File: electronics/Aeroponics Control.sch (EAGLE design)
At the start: 37 parts, among them IC1 7407N, K1 SRM-1C-SL-5VDC, K2 SRM-1C-SL-5VDC, Q1 FDU3N40TU, Q2 FDU3N40TU, Q3 FDU3N40TU, Q4 FDU3N40TU, Q6 FDU3N40TU, Q7 FDU3N40TU

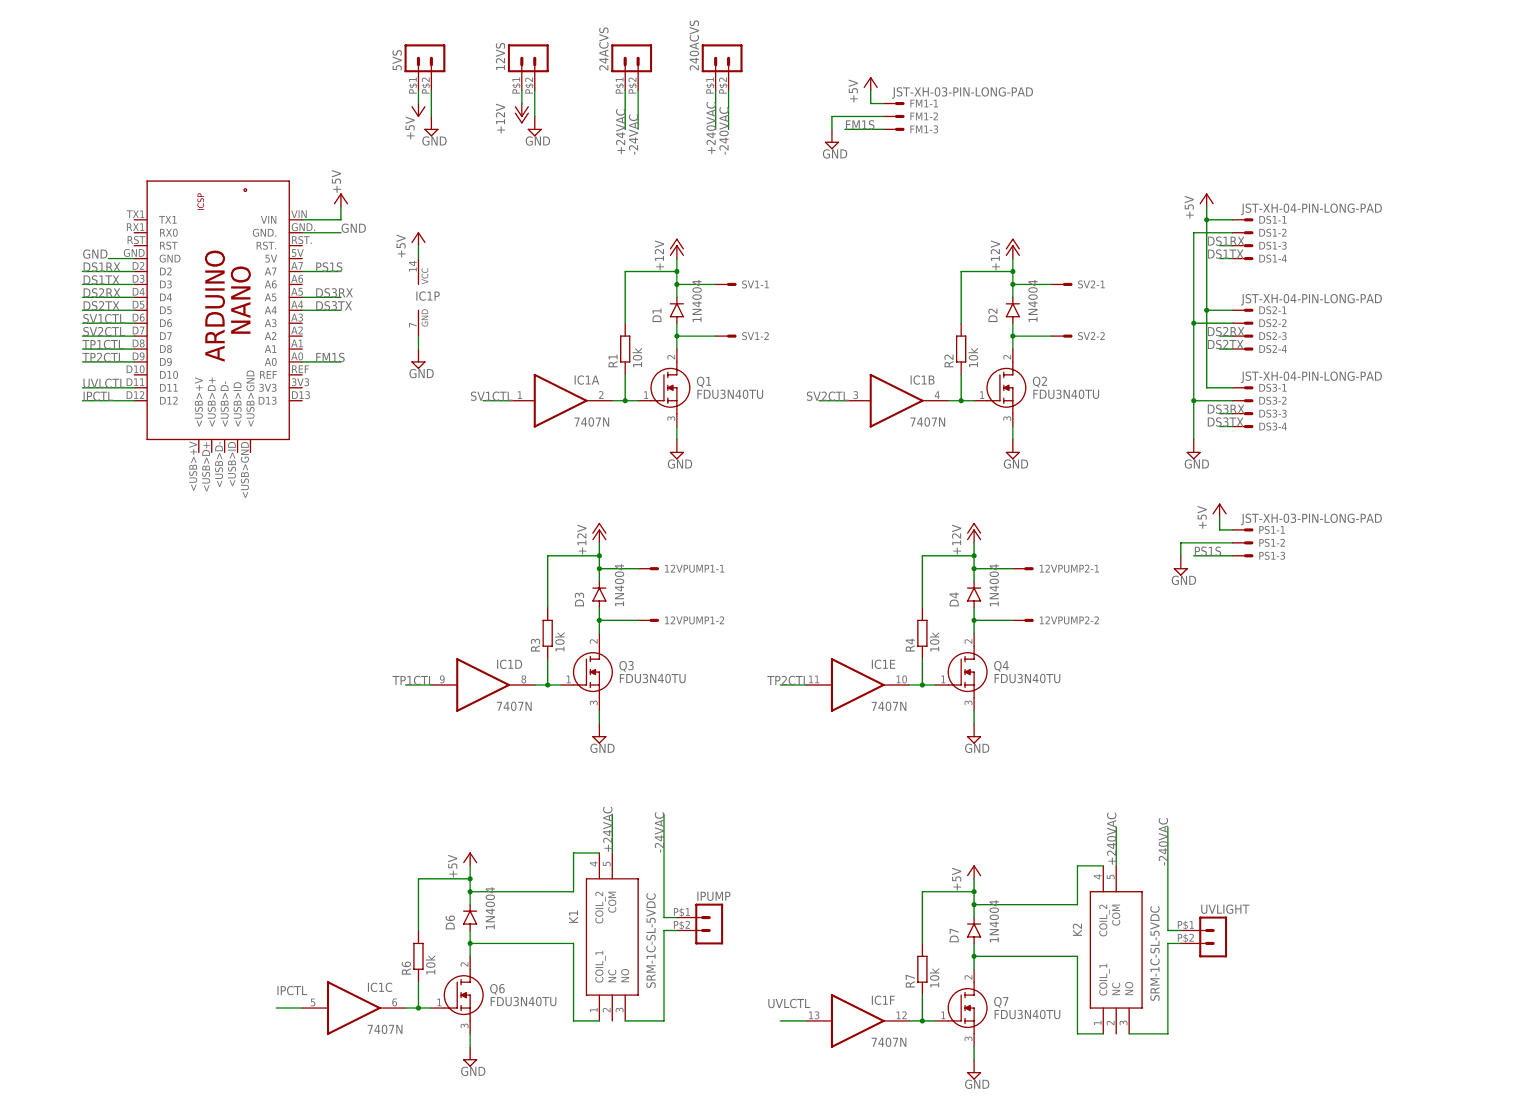
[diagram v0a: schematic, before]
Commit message: Electronics tested. Added calibration and debug.
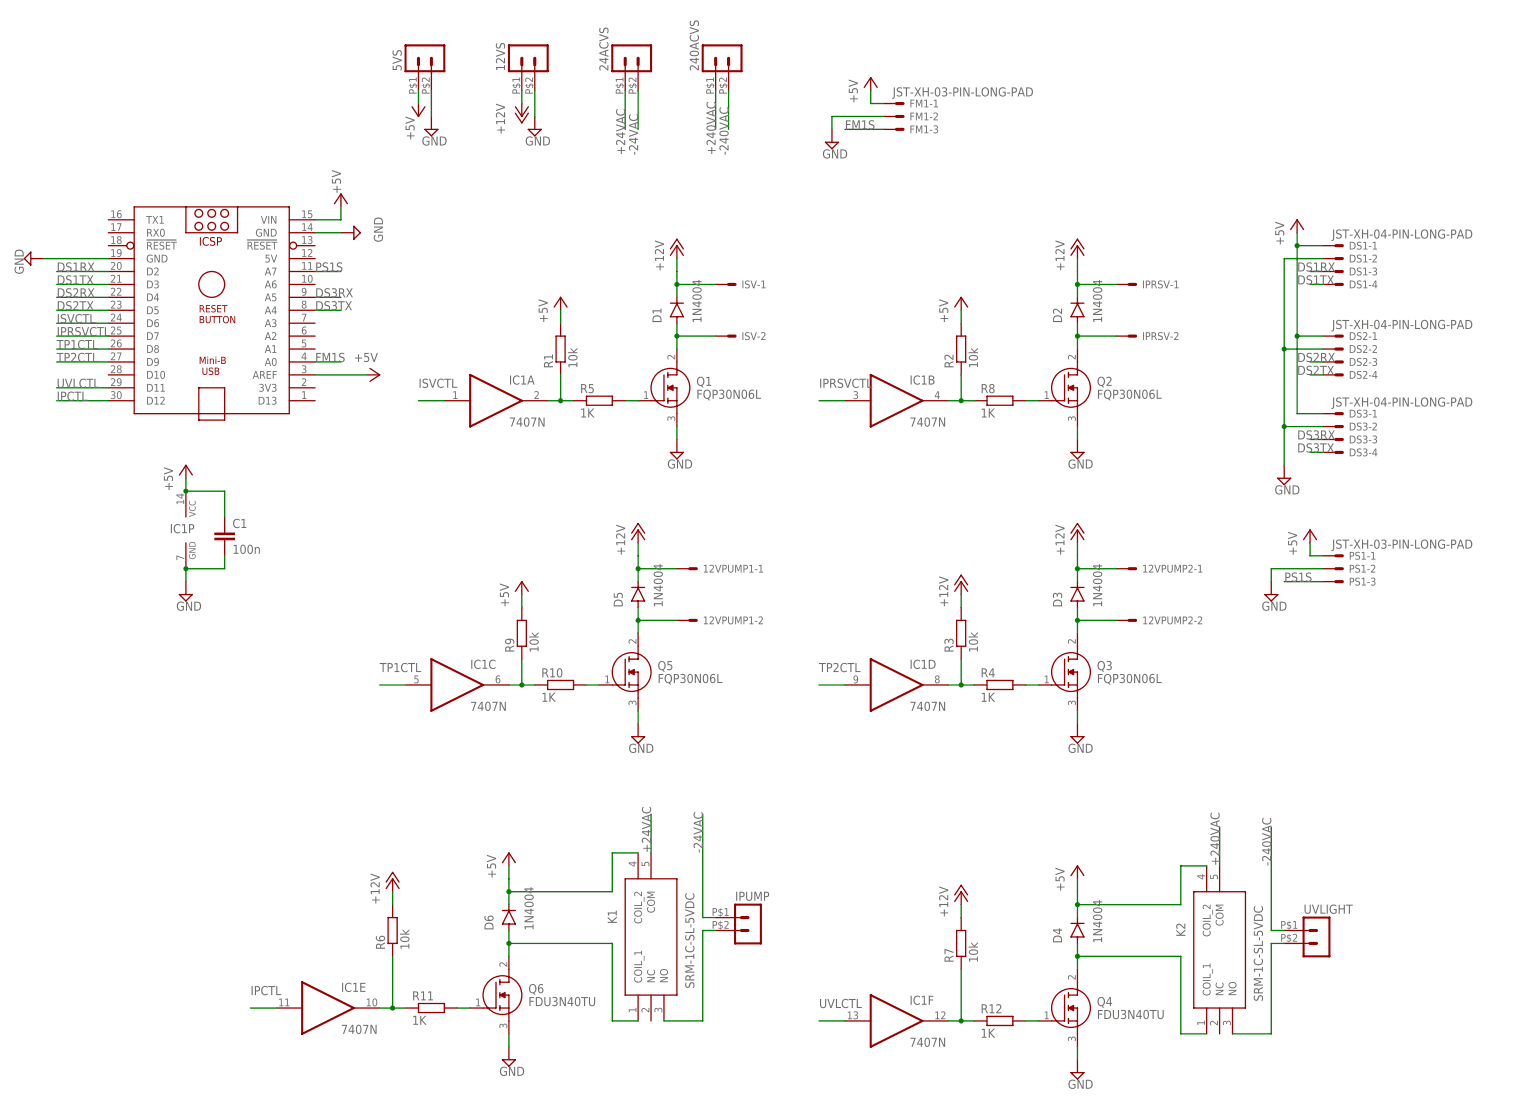
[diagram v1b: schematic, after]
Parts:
- removed D7: 1N4004, diode:1N4004
- removed Q7: FDU3N40TU, SamacSys_Parts:FDU3N40TU
- removed SV1, SV2: JST-XH-02-PIN-LONG-PAD, Rembrandt Electronics - JST XH Connectors v1-0:JST-XH-02-PIN-LONG-PAD
- added C1: 100n, Aeroponics Control:C-EU050-024X044
- added D5: 1N4004, Aeroponics Control:1N4004
- added IPRSV, ISV: JST-XH-02-PIN-LONG-PAD, Aeroponics Control:JST-XH-02-PIN-LONG-PAD
- added Q5: FQP30N06L, Aeroponics Control:FQP30N06L
- added R10, R11, R12, R5, R8: 1K, Aeroponics Control:R-EU_0204/7
- added R9: 10k, Aeroponics Control:R-EU_0204/7
- 12VPUMP1, 12VPUMP2: device Rembrandt Electronics - JST XH Connectors v1-0:JST-XH-02-PIN-LONG-PAD -> Aeroponics Control:JST-XH-02-PIN-LONG-PAD
- 12VS, 240ACVS, 24ACVS, 5VS, IPUMP, UVLIGHT: device con-molex-micro-fit-3_0:HEADER_POS2_43650-0215 -> Aeroponics Control:HEADER_POS2_43650-0215
- D1, D2, D3, D4, D6: device diode:1N4004 -> Aeroponics Control:1N4004
- DS1, DS2, DS3: device Rembrandt Electronics - JST XH Connectors v1-0:JST-XH-04-PIN-LONG-PAD -> Aeroponics Control:JST-XH-04-PIN-LONG-PAD
- FM1, PS1: device Rembrandt Electronics - JST XH Connectors v1-0:JST-XH-03-PIN-LONG-PAD -> Aeroponics Control:JST-XH-03-PIN-LONG-PAD
- IC1: device 74xx-eu:7407N -> Aeroponics Control:7407N
- K1, K2: device SamacSys_Parts:SRM-1C-SL-5VDC -> Aeroponics Control:SRM-1C-SL-5VDC
- PCB1: device E14_Arduino_revC:ARDUINO_NANOARDUINO_NANO_HEADERS -> Aeroponics Control:ARDUINO_NANO
- Q1, Q2, Q3: value FDU3N40TU -> FQP30N06L; device SamacSys_Parts:FDU3N40TU -> Aeroponics Control:FQP30N06L
- Q4, Q6: device SamacSys_Parts:FDU3N40TU -> Aeroponics Control:FDU3N40TU
- R1, R2, R3, R6, R7: device resistor:R-EU_0204/7 -> Aeroponics Control:R-EU_0204/7
- R4: value 10k -> 1K; device resistor:R-EU_0204/7 -> Aeroponics Control:R-EU_0204/7
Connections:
- net SV1CTL renamed ISVCTL
- net SV2CTL renamed IPRSVCTL
- removed net N$23: IC1C.O, Q6.G, R6.1
- removed net N$8 (its old number): IC1F.O, Q7.G, R7.1
- new net N$14: 12VPUMP1-2.S, D5.A, Q5.D
- new net N$15: IC1C.O, R10.1, R9.1
- new net N$16: Q5.G, R10.2
- new net N$17: IC1E.O, R11.1, R6.1
- new net N$18: Q4.G, R12.2
- new net N$19: IC1F.O, R12.1, R7.1
- new net N$5: Q1.G, R5.2
- new net N$9: IC1B.O, R2.1, R8.1
- net +12V: now also D5.C, IPRSV-1.S, ISV-1.S, R6.2, R7.2; no longer D4.C, R1.2, R2.2, R3.2, R4.2, SV1-1.S, SV2-1.S
- net +5V: now also C1.1, D4.C, PCB1.AREF, R1.2, R2.2, R3.2, R9.2; no longer D7.C, R6.2, R7.2
- net GND: now also C1.2, PCB1.GND@1, PCB1.GND@2, Q5.S; no longer PCB1.GND, PCB1.GND., Q7.S
- net IPCTL: now also IC1E.I; no longer IC1C.I
- net N$1: now also IPRSV-2.S; no longer SV2-2.S
- net N$10: now also ISV-2.S; no longer SV1-2.S
- net N$11: now also IC1D.O, R3.1, R4.1; no longer 12VPUMP1-2.S, D3.A, Q3.D
- net N$12: now also R4.2; no longer IC1D.O, R3.1
- net N$13: now also Q6.G, R11.2; no longer 12VPUMP2-2.S, D4.A, Q4.D
- net N$2: now also 12VPUMP2-2.S, D3.A, Q3.D; no longer IC1E.O, Q4.G, R4.1
- net N$3: now also R5.1; no longer Q1.G
- net N$4: now also R8.2; no longer IC1B.O, R2.1
- net N$6: now also D4.A, Q4.D; no longer D7.A, Q7.D
- net TP1CTL: now also IC1C.I; no longer IC1D.I
- net TP2CTL: now also IC1D.I; no longer IC1E.I
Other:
- moved on the sheet: 12VPUMP1-1, 12VPUMP1-2, 12VPUMP2-1, 12VPUMP2-2, DS1-1, DS1-2, DS1-3, DS1-4, DS2-1, DS2-2, DS2-3, DS2-4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

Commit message: Updated aeroponics control electronics.
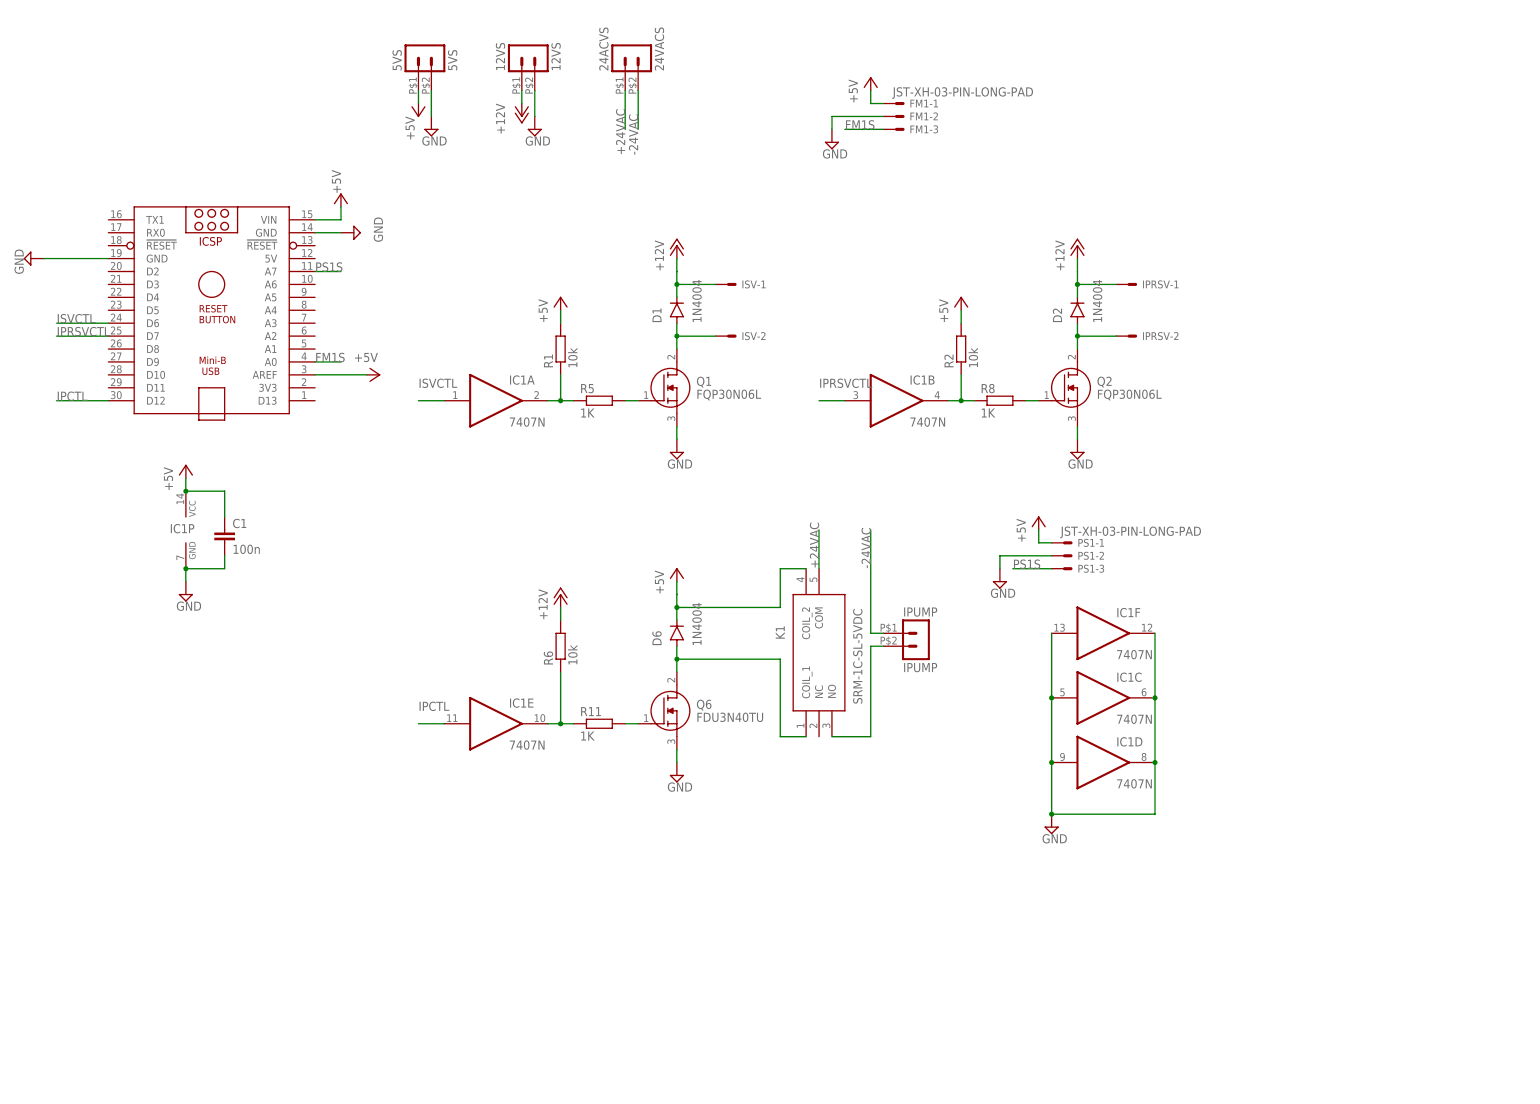
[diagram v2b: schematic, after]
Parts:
- removed 12VPUMP1, 12VPUMP2: JST-XH-02-PIN-LONG-PAD, Aeroponics Control:JST-XH-02-PIN-LONG-PAD
- removed 240ACVS, UVLIGHT: (no value), Aeroponics Control:HEADER_POS2_43650-0215
- removed D3, D4, D5: 1N4004, Aeroponics Control:1N4004
- removed DS1, DS2, DS3: JST-XH-04-PIN-LONG-PAD, Aeroponics Control:JST-XH-04-PIN-LONG-PAD
- removed K2: SRM-1C-SL-5VDC, Aeroponics Control:SRM-1C-SL-5VDC
- removed Q3, Q5: FQP30N06L, Aeroponics Control:FQP30N06L
- removed Q4: FDU3N40TU, Aeroponics Control:FDU3N40TU
- removed R10, R12, R4: 1K, Aeroponics Control:R-EU_0204/7
- removed R3, R7, R9: 10k, Aeroponics Control:R-EU_0204/7
- 12VS: value (none) -> 12VS
- 24ACVS: value (none) -> 24VACS
- 5VS: value (none) -> 5VS
- IPUMP: value (none) -> IPUMP
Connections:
- removed net +240VAC: 240ACVS.1, K2.COM
- removed net -240VAC: 240ACVS.2, UVLIGHT.1
- removed net DS1RX: DS1-3.S, PCB1.D2
- removed net DS1TX: DS1-4.S, PCB1.D3
- removed net DS2RX: DS2-3.S, PCB1.D4
- removed net DS2TX: DS2-4.S, PCB1.D5
- removed net DS3RX: DS3-3.S, PCB1.A5
- removed net DS3TX: DS3-4.S, PCB1.A4
- removed net N$11: IC1D.O, R3.1, R4.1
- removed net N$12: Q3.G, R4.2
- removed net N$14: 12VPUMP1-2.S, D5.A, Q5.D
- removed net N$15: IC1C.O, R10.1, R9.1
- removed net N$16: Q5.G, R10.2
- removed net N$18: Q4.G, R12.2
- removed net N$19: IC1F.O, R12.1, R7.1
- removed net N$2: 12VPUMP2-2.S, D3.A, Q3.D
- removed net N$6: D4.A, K2.COIL_1, Q4.D
- removed net N$8: K2.NO, UVLIGHT.2
- removed net TP1CTL: IC1C.I, PCB1.D8
- removed net TP2CTL: IC1D.I, PCB1.D9
- removed net UVLCTL: IC1F.I, PCB1.D11
- net +12V: no longer 12VPUMP1-1.S, 12VPUMP2-1.S, D3.C, D5.C, R7.2
- net +5V: no longer D4.C, DS1-1.S, DS2-1.S, DS3-1.S, K2.COIL_2, R3.2, R9.2
- net GND: now also IC1C.I, IC1C.O, IC1D.I, IC1D.O, IC1F.I, IC1F.O; no longer DS1-2.S, DS2-2.S, DS3-2.S, Q3.S, Q4.S, Q5.S
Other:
- moved on the sheet: D6, IC1C, IC1D, IC1E, IC1F, IPUMP, K1, PS1-1, PS1-2, PS1-3, Q6, R11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

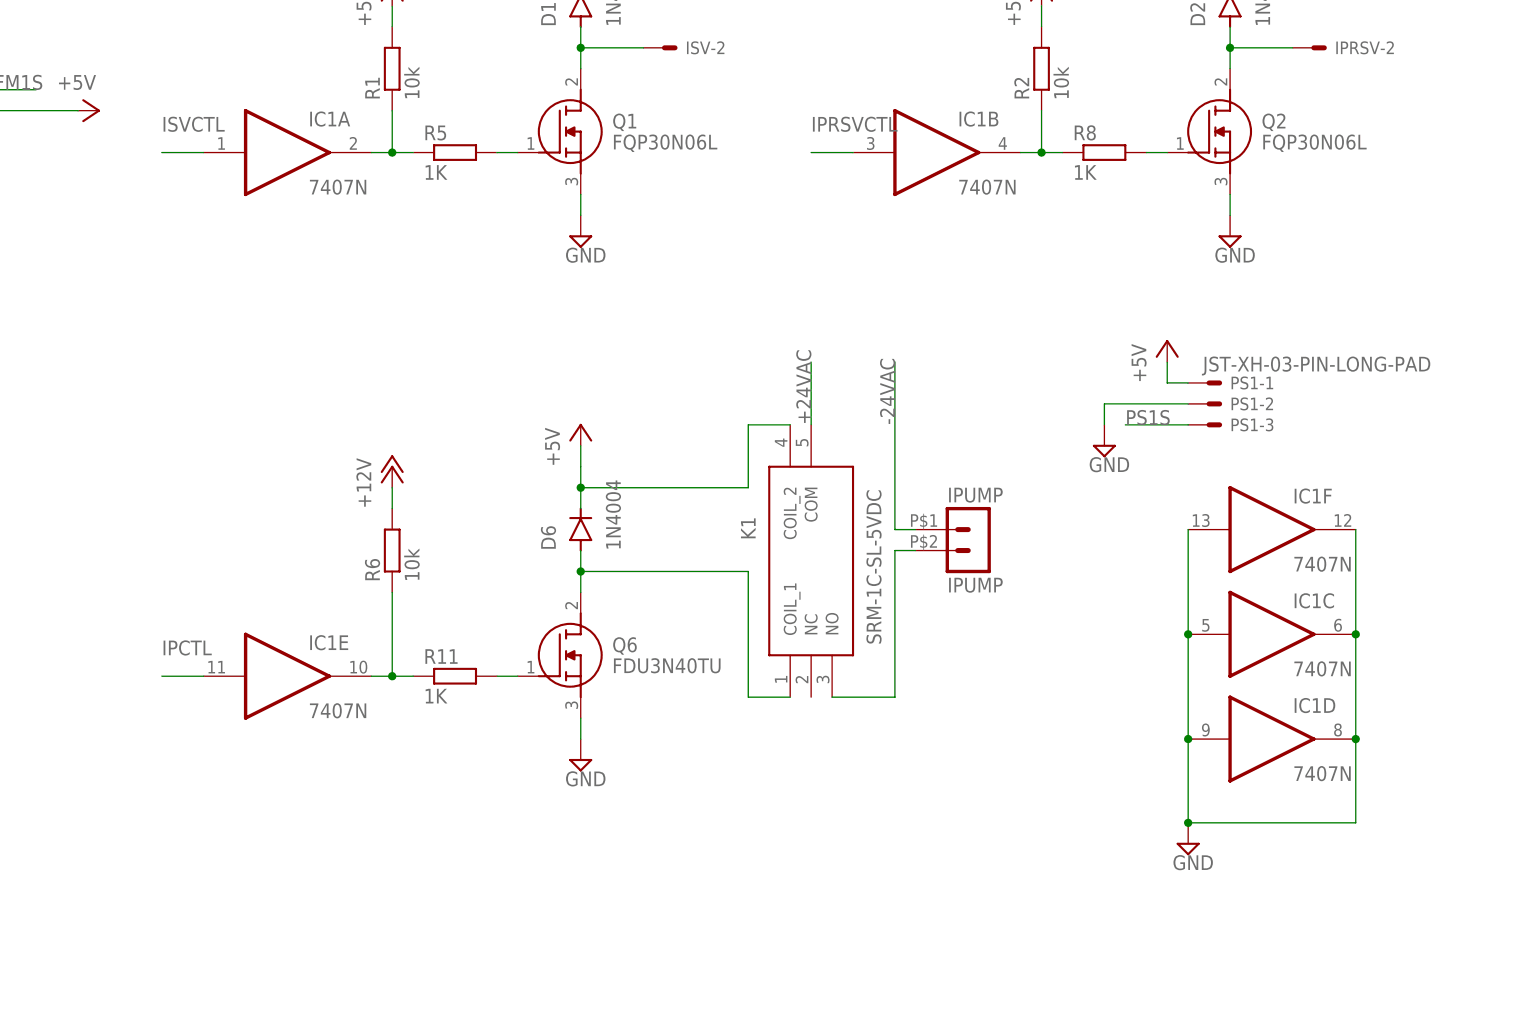
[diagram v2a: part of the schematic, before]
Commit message: Added pull down resistors to Arduino output pins
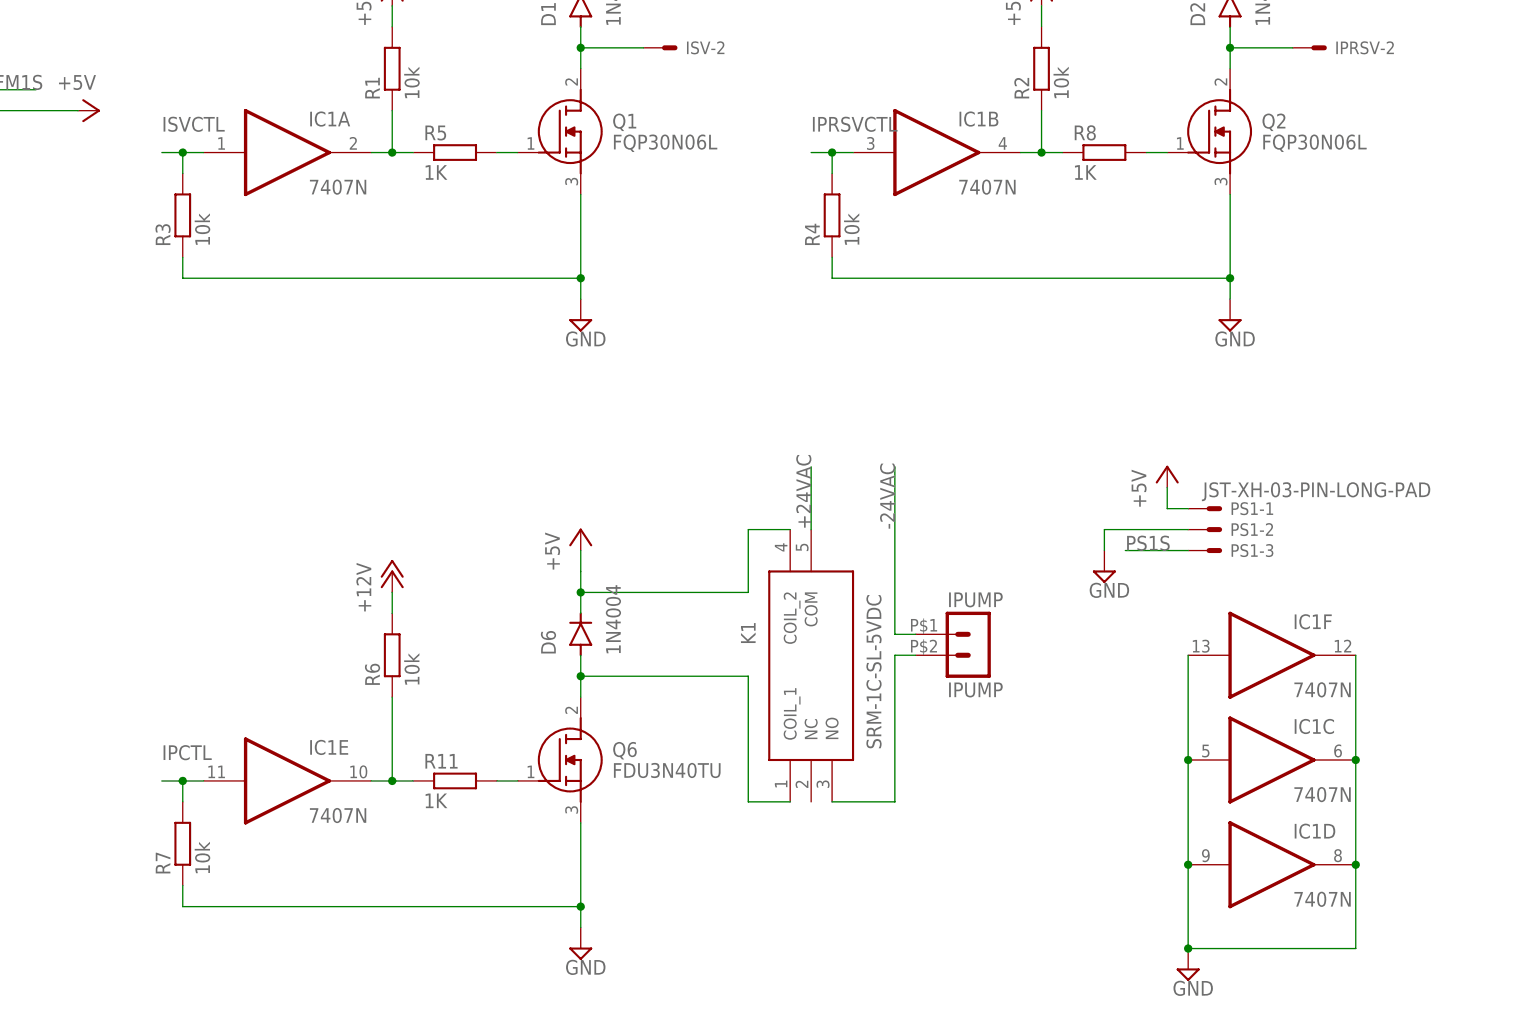
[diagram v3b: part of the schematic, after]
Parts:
- added R3, R4, R7: 10k, Aeroponics Control:R-EU_0204/7
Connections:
- net GND: now also R3.1, R4.1, R7.1
- net IPCTL: now also R7.2
- net IPRSVCTL: now also R4.2
- net ISVCTL: now also R3.2
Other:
- moved on the sheet: D6, IC1C, IC1D, IC1E, IC1F, IPUMP, K1, PS1-1, PS1-2, PS1-3, Q6, R11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
